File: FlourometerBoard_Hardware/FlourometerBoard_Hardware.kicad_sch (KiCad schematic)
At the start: 13 parts, among them J1 RJ45_LED_Shielded, U1 Teensy4.1_DEV-16771, U3 OKI

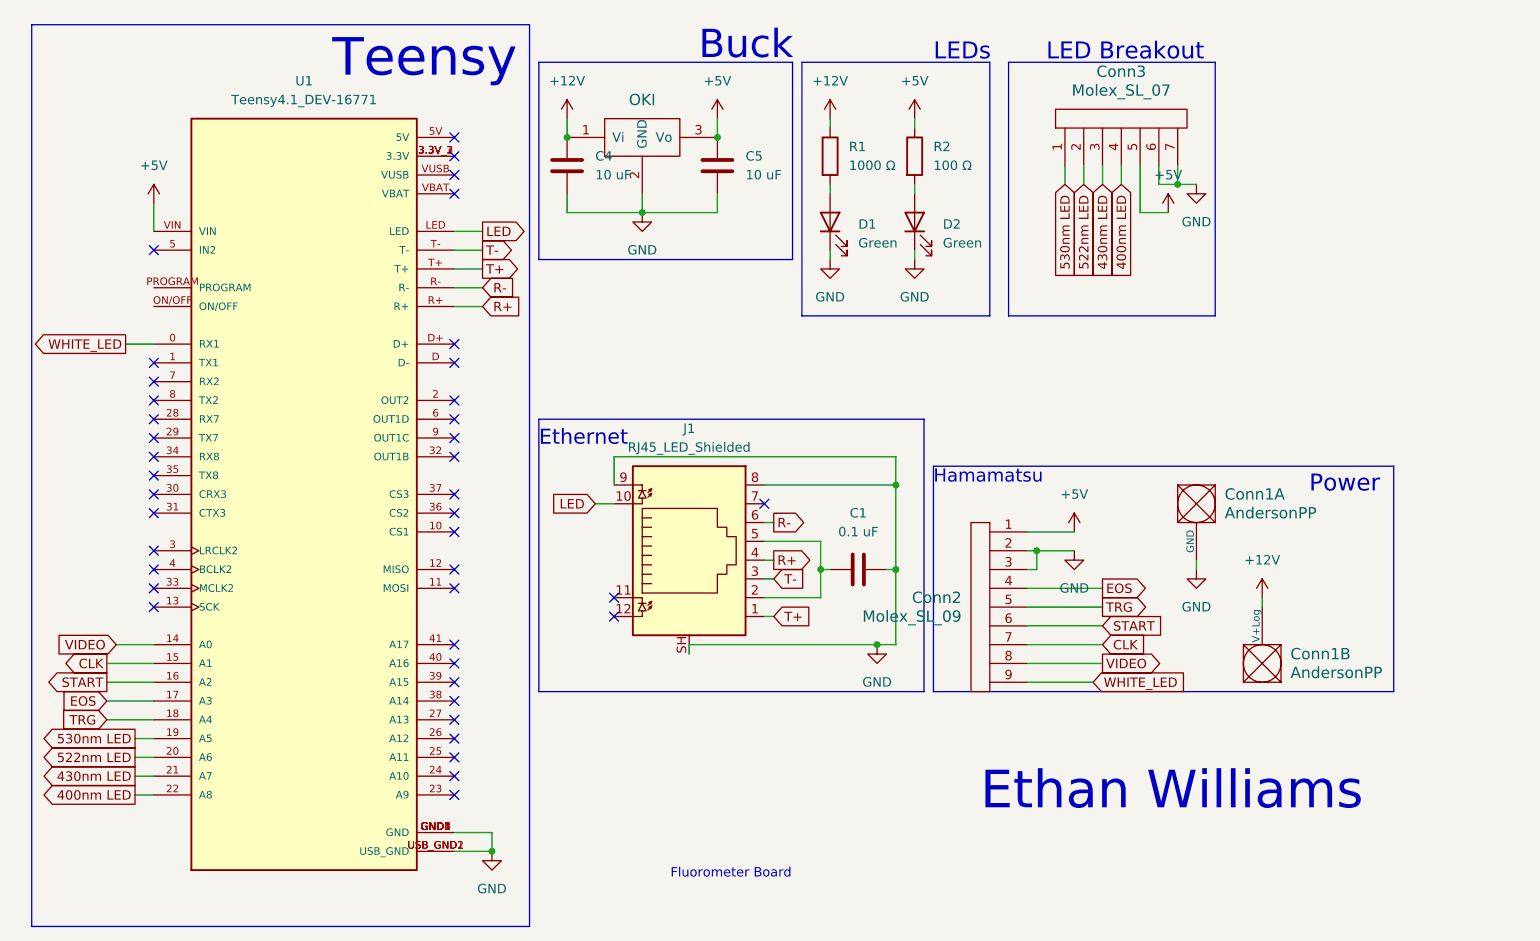
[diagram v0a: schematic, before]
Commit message: Changes made based on layout review notes
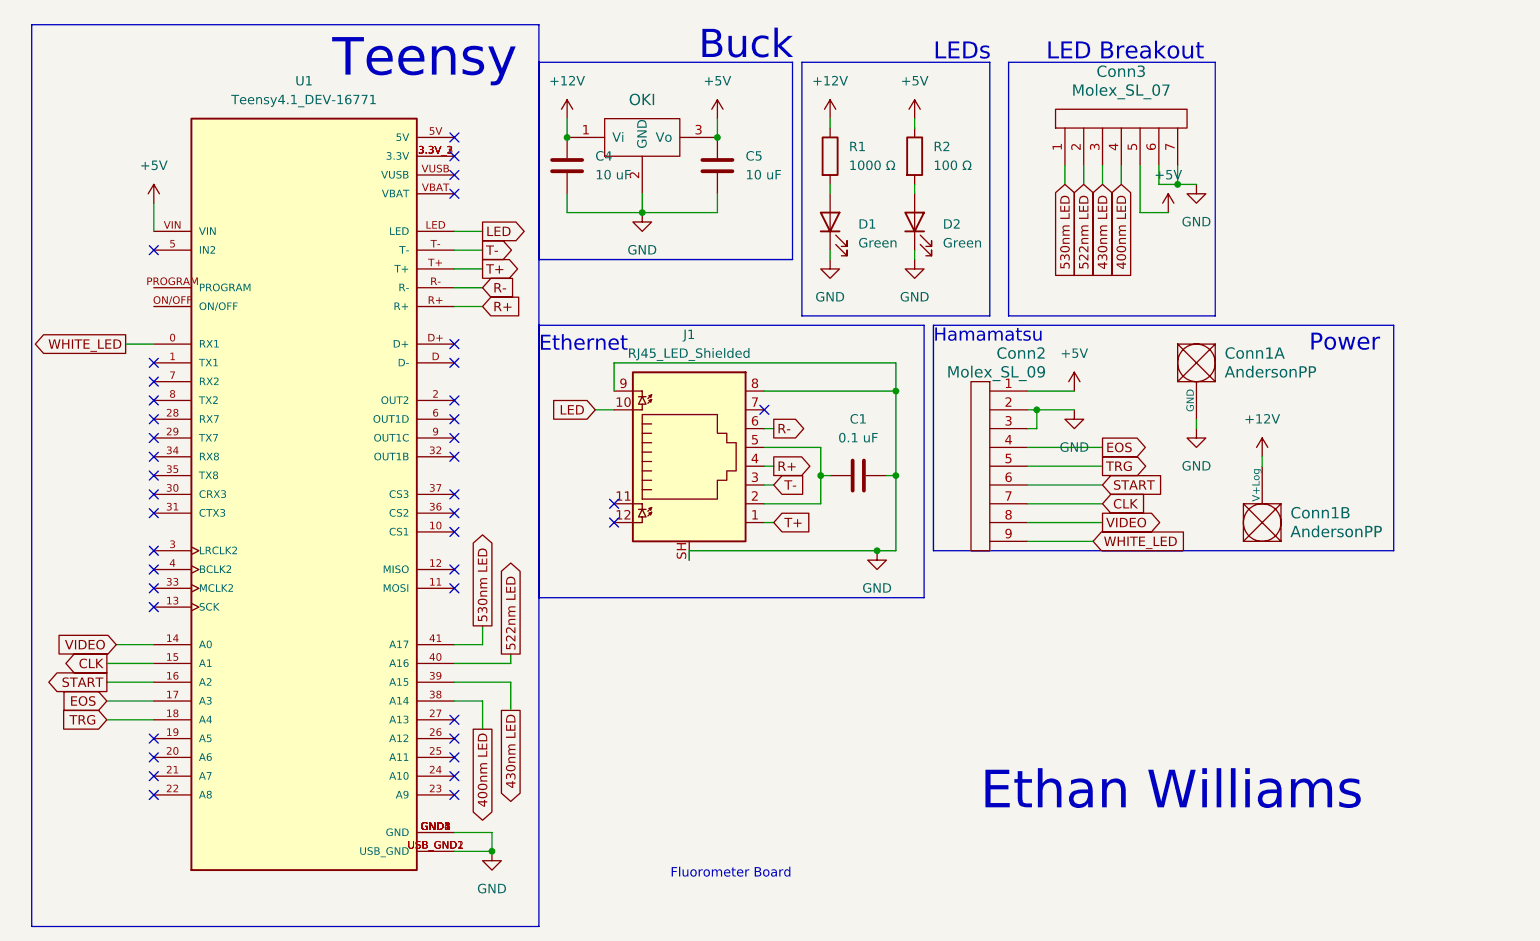
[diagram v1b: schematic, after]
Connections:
- net 400nm LED: now also U1.38 (A14); no longer U1.22 (A8)
- net 430nm LED: now also U1.39 (A15); no longer U1.21 (A7)
- net 522nm LED: now also U1.40 (A16); no longer U1.20 (A6)
- net 530nm LED: now also U1.41 (A17); no longer U1.19 (A5)
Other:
- moved on the sheet: C1, Conn1A, Conn1B, Conn2, J1

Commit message: Changed Anderson Footprint from PV
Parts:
- Conn1: footprint MRDT_Connectors:Square_Anderson_2_H_Side_By_Side_PV -> MRDT_Connectors:Square_Anderson_2_H_Side_By_Side
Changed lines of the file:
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@@
       (effects (font (size 1.524 1.524)) (justify left))
     )
-    (property "Footprint" "MRDT_Connectors:Square_Anderson_2_H_Side_By_Side_PV" (at 153.67 52.07 0)
+    (property "Footprint" "MRDT_Connectors:Square_Anderson_2_H_Side_By_Side" (at 153.67 52.07 0)
       (effects (font (size 1.524 1.524)) hide)
     )
@@
       (effects (font (size 1.524 1.524)) (justify right))
     )
-    (property "Footprint" "MRDT_Connectors:Square_Anderson_2_H_Side_By_Side_PV" (at 195.58 86.36 0)
+    (property "Footprint" "MRDT_Connectors:Square_Anderson_2_H_Side_By_Side" (at 195.58 86.36 0)
       (effects (font (size 1.524 1.524)) hide)
     )

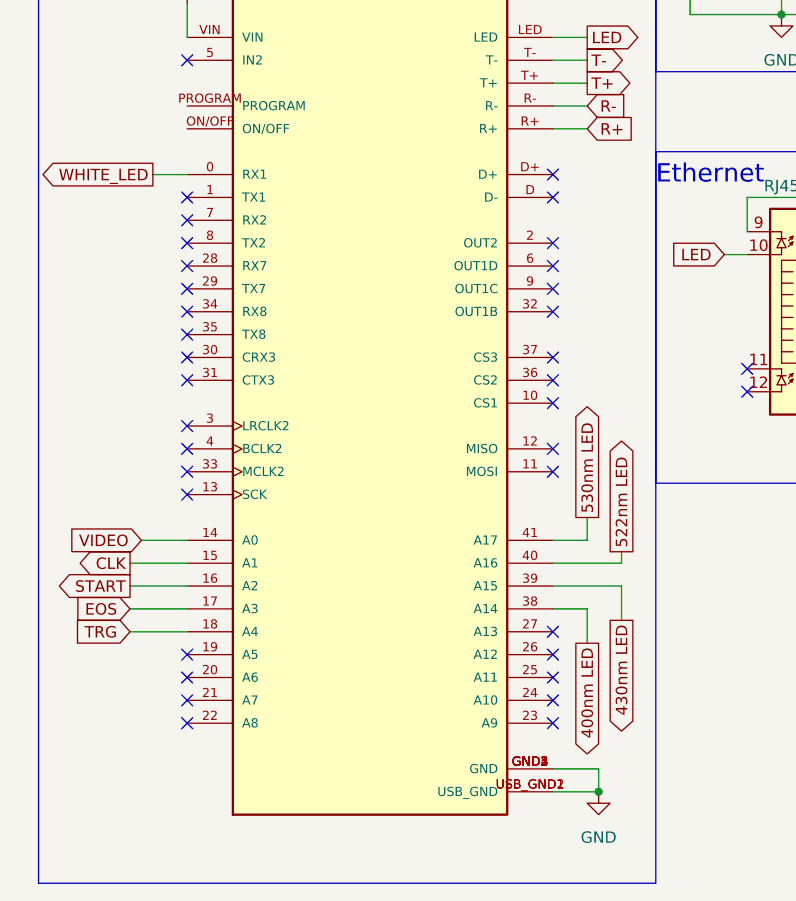
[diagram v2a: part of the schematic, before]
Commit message: Added Pull Down Resistors to MOSFETs
And some other things
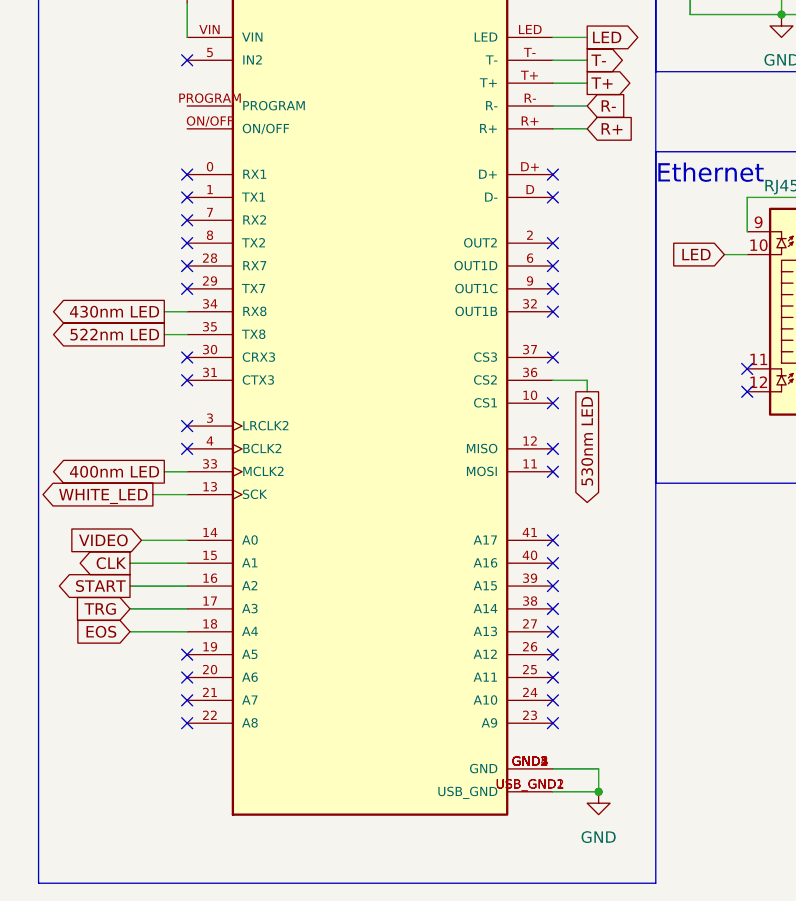
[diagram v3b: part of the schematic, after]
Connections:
- net 400nm LED: now also U1.33 (MCLK2); no longer U1.38 (A14)
- net 430nm LED: now also U1.34 (RX8); no longer U1.39 (A15)
- net 522nm LED: now also U1.35 (TX8); no longer U1.40 (A16)
- net 530nm LED: now also U1.36 (CS2); no longer U1.41 (A17)
- net EOS: now also U1.18 (A4); no longer U1.17 (A3)
- net TRG: now also U1.17 (A3); no longer U1.18 (A4)
- net WHITE_LED: now also U1.13 (SCK); no longer U1.0 (RX1)
